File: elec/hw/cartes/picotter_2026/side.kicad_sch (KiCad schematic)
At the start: 18 parts, among them J3 5264-3P, J4 22053051, J5 22053051, J6 22053041, J7 22053051, U2 VCNL4040M3OE

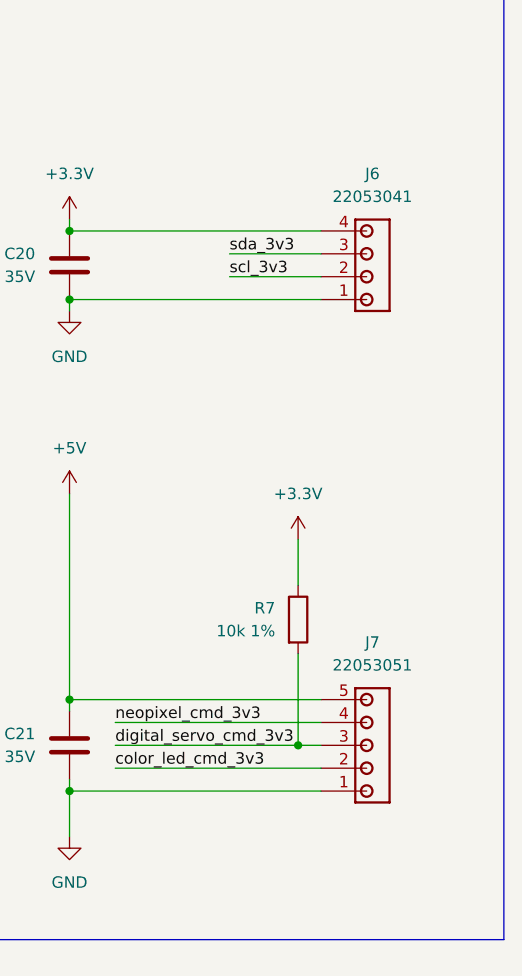
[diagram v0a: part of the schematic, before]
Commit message: pictotter: schematic fixes after review. New prelayout proposition
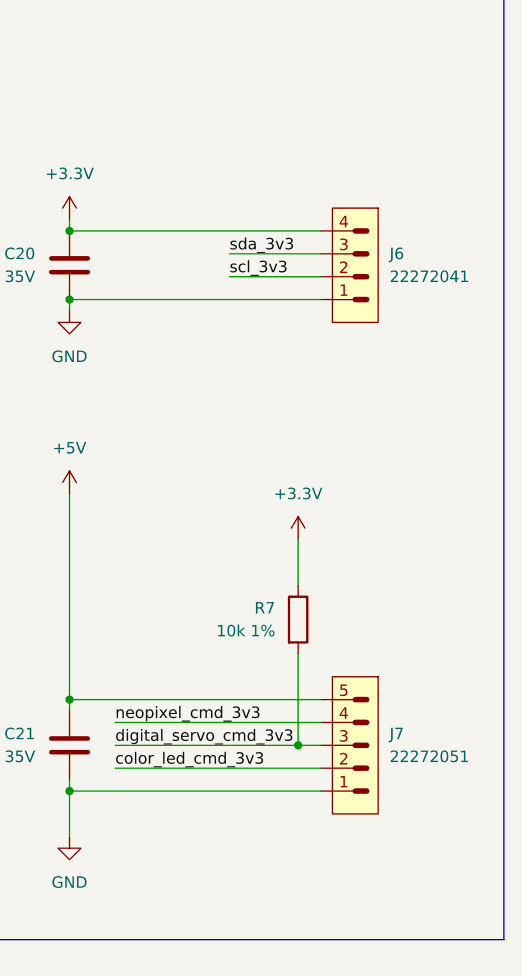
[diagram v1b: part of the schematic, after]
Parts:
- removed J6: 22053041, cocotter_connectors:22053041, symbol cocotter_connectors:22053041
- removed J7: 22053051, cocotter_connectors:22053051, symbol cocotter_connectors:22053051
- added J6: 22272041, cocotter_connectors:22272041, symbol cocotter_connectors:22272041
- added J7: 22272051, cocotter_connectors:22272051, symbol cocotter_connectors:22272051
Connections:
- net +3.3V: now also J6.4
- net +5V: now also J7.5
- net GND: now also J6.1, J7.1
- net color_led_cmd_3v3: now also J7.2
- net digital_servo_cmd_3v3: now also J7.3
- net neopixel_cmd_3v3: now also J7.4
- net scl_3v3: now also J6.2
- net sda_3v3: now also J6.3
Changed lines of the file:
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@@
-	)
-	(symbol
-		(lib_id "cocotter_connectors:22053041")
-		(at 240.03 46.99 0)
-		(mirror y)
-		(unit 1)
-		(exclude_from_sim no)
-		(in_bom yes)
-		(on_board yes)
-		(dnp no)
-		(fields_autoplaced yes)
-		(property "Reference" "J6"
-			(at 245.745 38.1 0)
-			(effects
-				(font
-					(size 1.27 1.27)
-				)
-			)
-		)
-		(property "Value" "22053041"
-			(at 245.745 40.64 0)
-			(effects
-				(font
-					(size 1.27 1.27)
-				)
-			)
-		)
-		(property "Footprint" "cocotter_connectors:22053041"
-			(at 240.03 46.99 0)
-			(effects
-				(font
-					(size 1.27 1.27)
-				)
-				(hide yes)
-			)
-		)
-		(property "Datasheet" ""
-			(at 240.03 46.99 0)
-			(effects
-				(font
-					(size 1.27 1.27)
-				)
-				(hide yes)
-			)
-		)
-		(property "Description" "mini KK, 2.54mm pitch, 4 ways, right angle"
-			(at 240.03 46.99 0)
-			(effects
-				(font
-					(size 1.27 1.27)
-				)
-				(hide yes)
-			)
-		)
-		(property "JLCPCB Part #" "C5271241"
-			(at 240.03 46.99 0)
-			(effects
-				(font
-					(size 1.27 1.27)
-				)
-				(hide yes)
-			)
-		)
-		(pin "4"
-		)
-		(pin "3"
-		)
-		(pin "1"
-		)
-		(pin "2"
-		)
-		(instances
-			(project "picotter_2026"
-				(path "/a7992a71-8976-4fb0-bae5-4423ba97b789/3f9fae8c-4d49-41b9-91f7-d02e6503a994"
-					(reference "J16")
-					(unit 1)
-				)
-				(path "/a7992a71-8976-4fb0-bae5-4423ba97b789/b39db1aa-64f6-4967-b8af-1731839ee66d"
-					(reference "J11")
-					(unit 1)
-				)
-				(path "/a7992a71-8976-4fb0-bae5-4423ba97b789/c723ae89-944f-486c-b5ab-f52577eee63d"
-					(reference "J6")
-					(unit 1)
-				)
-			)
-		)
 	)
 	(symbol
@@
 	)
 	(symbol
+		(lib_id "cocotter_connectors:22272041")
+		(at 240.03 49.53 0)
+		(mirror y)
+		(unit 1)
+		(exclude_from_sim no)
+		(in_bom yes)
+		(on_board yes)
+		(dnp no)
+		(fields_autoplaced yes)
+		(property "Reference" "J6"
+			(at 247.65 46.9899 0)
+			(effects
+				(font
+					(size 1.27 1.27)
+				)
+				(justify right)
+			)
+		)
+		(property "Value" "22272041"
+			(at 247.65 49.5299 0)
+			(effects
+				(font
+					(size 1.27 1.27)
+				)
+				(justify right)
+			)
+		)
+		(property "Footprint" "cocotter_connectors:22272041"
+			(at 243.332 61.468 0)
+			(effects
+				(font
+					(size 1.27 1.27)
+				)
+				(hide yes)
+			)
+		)
+		(property "Datasheet" "https://www.molex.com/en-us/products/part-detail/22272041"
+			(at 240.03 58.42 0)
+			(effects
+				(font
+					(size 1.27 1.27)
+				)
+				(hide yes)
+			)
+		)
+		(property "Description" "mini kk 4 voies vertical"
+			(at 240.03 58.42 0)
+			(effects
+				(font
+					(size 1.27 1.27)
+				)
+				(hide yes)
+			)
+		)
+		(property "JLCPCB Part #" "C504991"
+			(at 240.03 49.53 0)
+			(effects
+				(font
+					(size 1.27 1.27)
+				)
+				(hide yes)
+			)
+		)
+		(pin "2"
+		)
+		(pin "1"
+		)
+		(pin "4"
+		)
+		(pin "3"
+		)
+		(instances
+			(project ""
+				(path "/a7992a71-8976-4fb0-bae5-4423ba97b789/3f9fae8c-4d49-41b9-91f7-d02e6503a994"
+					(reference "J16")
+					(unit 1)
+				)
+				(path "/a7992a71-8976-4fb0-bae5-4423ba97b789/b39db1aa-64f6-4967-b8af-1731839ee66d"
+					(reference "J11")
+					(unit 1)
+				)
+				(path "/a7992a71-8976-4fb0-bae5-4423ba97b789/c723ae89-944f-486c-b5ab-f52577eee63d"
+					(reference "J6")
+					(unit 1)
+				)
+			)
+		)
+	)
+	(symbol
 		(lib_id "cocotter_resistors:R_2k2_0603_1%")
 		(at 49.53 80.01 0)
@@
 	)
 	(symbol
-		(lib_id "cocotter_connectors:22053051")
-		(at 240.03 101.6 0)
-		(mirror y)
-		(unit 1)
-		(exclude_from_sim no)
-		(in_bom yes)
-		(on_board yes)
-		(dnp no)
-		(fields_autoplaced yes)
-		(property "Reference" "J7"
-			(at 245.745 90.17 0)
-			(effects
-				(font
-					(size 1.27 1.27)
-				)
-			)
-		)
-		(property "Value" "22053051"
-			(at 245.745 92.71 0)
-			(effects
-				(font
-					(size 1.27 1.27)
-				)
-			)
-		)
-		(property "Footprint" "cocotter_connectors:22053051"
-			(at 240.03 101.6 0)
-			(effects
-				(font
-					(size 1.27 1.27)
-				)
-				(hide yes)
-			)
-		)
-		(property "Datasheet" ""
-			(at 240.03 101.6 0)
-			(effects
-				(font
-					(size 1.27 1.27)
-				)
-				(hide yes)
-			)
-		)
-		(property "Description" "mini KK, 2.54mm pitch, 5ways, right angle"
-			(at 240.03 101.6 0)
-			(effects
-				(font
-					(size 1.27 1.27)
-				)
-				(hide yes)
-			)
-		)
-		(property "JLCPCB Part #" "C586992"
-			(at 240.03 101.6 0)
-			(effects
-				(font
-					(size 1.27 1.27)
-				)
-				(hide yes)
-			)
-		)
-		(pin "2"
-		)
-		(pin "1"
-		)
-		(pin "3"
-		)
-		(pin "4"
-		)
-		(pin "5"
-		)
-		(instances
-			(project "picotter_2026"
-				(path "/a7992a71-8976-4fb0-bae5-4423ba97b789/3f9fae8c-4d49-41b9-91f7-d02e6503a994"
-					(reference "J17")
-					(unit 1)
-				)
-				(path "/a7992a71-8976-4fb0-bae5-4423ba97b789/b39db1aa-64f6-4967-b8af-1731839ee66d"
-					(reference "J12")
-					(unit 1)
-				)
-				(path "/a7992a71-8976-4fb0-bae5-4423ba97b789/c723ae89-944f-486c-b5ab-f52577eee63d"
-					(reference "J7")
-					(unit 1)
-				)
-			)
-		)
-	)
-	(symbol
 		(lib_id "power:+6V")
 		(at 53.34 137.16 0)
@@
 					(unit 1)
 				)
+			)
+		)
+	)
+	(symbol
+		(lib_id "cocotter_connectors:22272051")
+		(at 240.03 101.6 0)
+		(mirror y)
+		(unit 1)
+		(exclude_from_sim no)
+		(in_bom yes)
+		(on_board yes)
+		(dnp no)
+		(fields_autoplaced yes)
+		(property "Reference" "J7"
+			(at 247.65 100.3299 0)
+			(effects
+				(font
+					(size 1.27 1.27)
+				)
+				(justify right)
+			)
+		)
+		(property "Value" "22272051"
+			(at 247.65 102.8699 0)
+			(effects
+				(font
+					(size 1.27 1.27)
+				)
+				(justify right)
+			)
+		)
+		(property "Footprint" "cocotter_connectors:22272051"
+			(at 243.332 113.538 0)
+			(effects
+				(font
+					(size 1.27 1.27)
+				)
+				(hide yes)
+			)
+		)
+		(property "Datasheet" "https://www.molex.com/en-us/products/part-detail/22272051"
+			(at 240.03 110.49 0)
+			(effects
+				(font
+					(size 1.27 1.27)
+				)
+				(hide yes)
+			)
+		)
+		(property "Description" "mini kk 5 voies vertical"
+			(at 240.03 110.49 0)
+			(effects
+				(font
+					(size 1.27 1.27)
+				)
+				(hide yes)
+			)
+		)
+		(property "JLCPCB Part #" "C585785"
+			(at 240.03 101.6 0)
+			(effects
+				(font
+					(size 1.27 1.27)
+				)
+				(hide yes)
+			)
+		)
+		(pin "3"
+		)
+		(pin "5"
+		)
+		(pin "1"
+		)
+		(pin "4"
+		)
+		(pin "2"
+		)
+		(instances
+			(project ""
+				(path "/a7992a71-8976-4fb0-bae5-4423ba97b789/3f9fae8c-4d49-41b9-91f7-d02e6503a994"
+					(reference "J17")
+					(unit 1)
+				)
+				(path "/a7992a71-8976-4fb0-bae5-4423ba97b789/b39db1aa-64f6-4967-b8af-1731839ee66d"
+					(reference "J12")
+					(unit 1)
+				)
+				(path "/a7992a71-8976-4fb0-bae5-4423ba97b789/c723ae89-944f-486c-b5ab-f52577eee63d"
+					(reference "J7")
+					(unit 1)
+				)

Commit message: picotter: final layout
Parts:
- U2: footprint cocotter_ic:VISHAY_VCNL4040_4X2X1.1 -> VCNL4040M3OE:VISHAY_VCNL4040_4X2X1.1
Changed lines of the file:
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@@
-	(wire
-		(pts
-			(xy 41.8506 21.59) (xy 68.5206 21.59)
-		)
-		(stroke
-			(width 0)
-			(type default)
-		)
-	)
 	(wire
 		(pts
@@
 	(wire
 		(pts
-			(xy 41.8506 24.13) (xy 68.5206 24.13)
-		)
-		(stroke
-			(width 0)
-			(type default)
-		)
-	)
-	(wire
-		(pts
 			(xy 19.05 95.25) (xy 41.91 95.25)
 		)
@@
 	(wire
 		(pts
-			(xy 41.8506 26.67) (xy 68.5206 26.67)
-		)
-		(stroke
-			(width 0)
-			(type default)
-		)
-	)
-	(wire
-		(pts
 			(xy 104.14 72.39) (xy 104.14 74.93)
 		)
@@
 	(wire
 		(pts
+			(xy 41.91 24.13) (xy 68.58 24.13)
+		)
+		(stroke
+			(width 0)
+			(type default)
+		)
+	)
+	(wire
+		(pts
 			(xy 237.49 101.6) (xy 240.03 101.6)
 		)
@@
 	(wire
 		(pts
+			(xy 41.91 21.59) (xy 68.58 21.59)
+		)
+		(stroke
+			(width 0)
+			(type default)
+		)
+	)
+	(wire
+		(pts
 			(xy 76.2 69.85) (xy 76.2 72.39)
 		)
@@
 		(pts
 			(xy 53.34 138.43) (xy 53.34 165.1)
+		)
+		(stroke
+			(width 0)
+			(type default)
+		)
+	)
+	(wire
+		(pts
+			(xy 41.91 26.67) (xy 68.58 26.67)
 		)
 		(stroke
@@
 	)
 	(label "irq_floor_3v3"
-		(at 68.5206 24.13 180)
+		(at 68.58 24.13 180)
 		(effects
 			(font
@@
 	)
 	(label "neopixel_cmd_3v3"
-		(at 68.5206 26.67 180)
+		(at 68.58 26.67 180)
 		(effects
 			(font
@@
 	)
 	(label "sda_3v3"
-		(at 68.5206 21.59 180)
+		(at 68.58 21.59 180)
 		(effects
 			(font
@@
 	(hierarchical_label "irq_floor_3v3"
 		(shape output)
-		(at 41.8506 24.13 180)
+		(at 41.91 24.13 180)
 		(effects
 			(font
@@
 	(hierarchical_label "neopixel_cmd_3v3"
 		(shape input)
-		(at 41.8506 26.67 180)
+		(at 41.91 26.67 180)
 		(effects
 			(font
@@
 	(hierarchical_label "sda_3v3"
 		(shape bidirectional)
-		(at 41.8506 21.59 180)
+		(at 41.91 21.59 180)
 		(effects
 			(font
@@
 			)
 		)
-		(property "Footprint" "cocotter_ic:VISHAY_VCNL4040_4X2X1.1"
+		(property "Footprint" "VCNL4040M3OE:VISHAY_VCNL4040_4X2X1.1"
 			(at 78.74 95.25 0)
 			(effects

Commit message: picotter: add led + 8 testpoints
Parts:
- U2: footprint VCNL4040M3OE:VISHAY_VCNL4040_4X2X1.1 -> cocotter_ic:VISHAY_VCNL4040_4X2X1.1
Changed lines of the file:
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@@
 			)
 		)
-		(property "Footprint" "VCNL4040M3OE:VISHAY_VCNL4040_4X2X1.1"
+		(property "Footprint" "cocotter_ic:VISHAY_VCNL4040_4X2X1.1"
 			(at 78.74 95.25 0)
 			(effects

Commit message: picotter: 3v3 to 5v translator added to neopixel cmd signal. schematic and pcb modified.
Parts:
- added C38, C69: 100nF 50V, cocotter_capacitors:C_0603_1608Metric, symbol cocotter_capacitors:C_100nF_50V_0603
- added R55: 10k 1%, cocotter_resistor:r0603_reflow, symbol cocotter_resistors:R_10k_0603_1%
- added U9: SN74LVC1T45DBV, Package_TO_SOT_SMD:SOT-23-6, symbol cocotter_ic:SN74LVC1T45DBV
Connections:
- net +3.3V: now also C38.1, R55.1, U9.1 (VCCA)
- net +5V: now also C69.1, U9.6 (VCCB)
- net GND: now also C38.2, C69.2, U9.2 (GND)
- net neopixel_cmd_3v3: now also U9.3 (A); no longer J7.4
- new net: R55.2, U9.5 (DIR)
- new net neopixel_cmd_5v: J7.4, U9.4 (B)
